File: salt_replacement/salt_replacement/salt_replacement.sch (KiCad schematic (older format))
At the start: 20 parts, among them J1 SALT chip package pins, Q1 MMBT9014C, U1 LM2596S-5, U2 MAX3232, U3 LM393

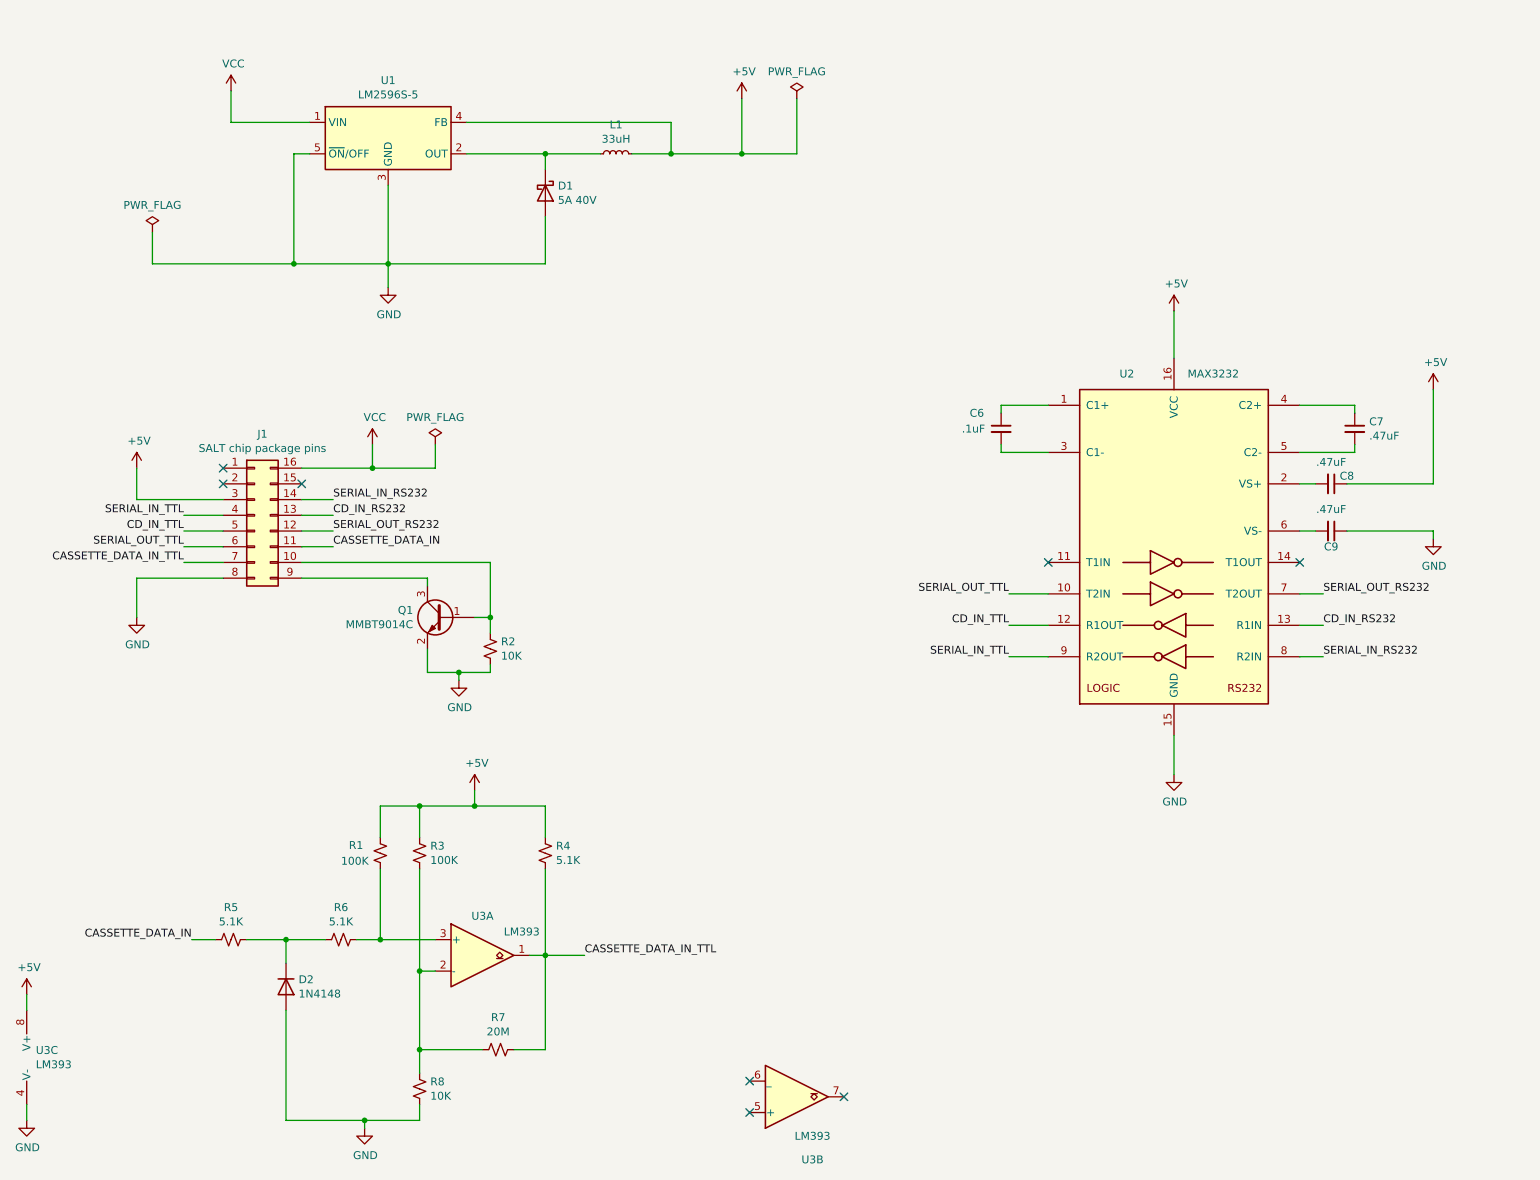
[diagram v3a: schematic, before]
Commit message: cleaned up schematic, added comments and added a PDF version of the schematic
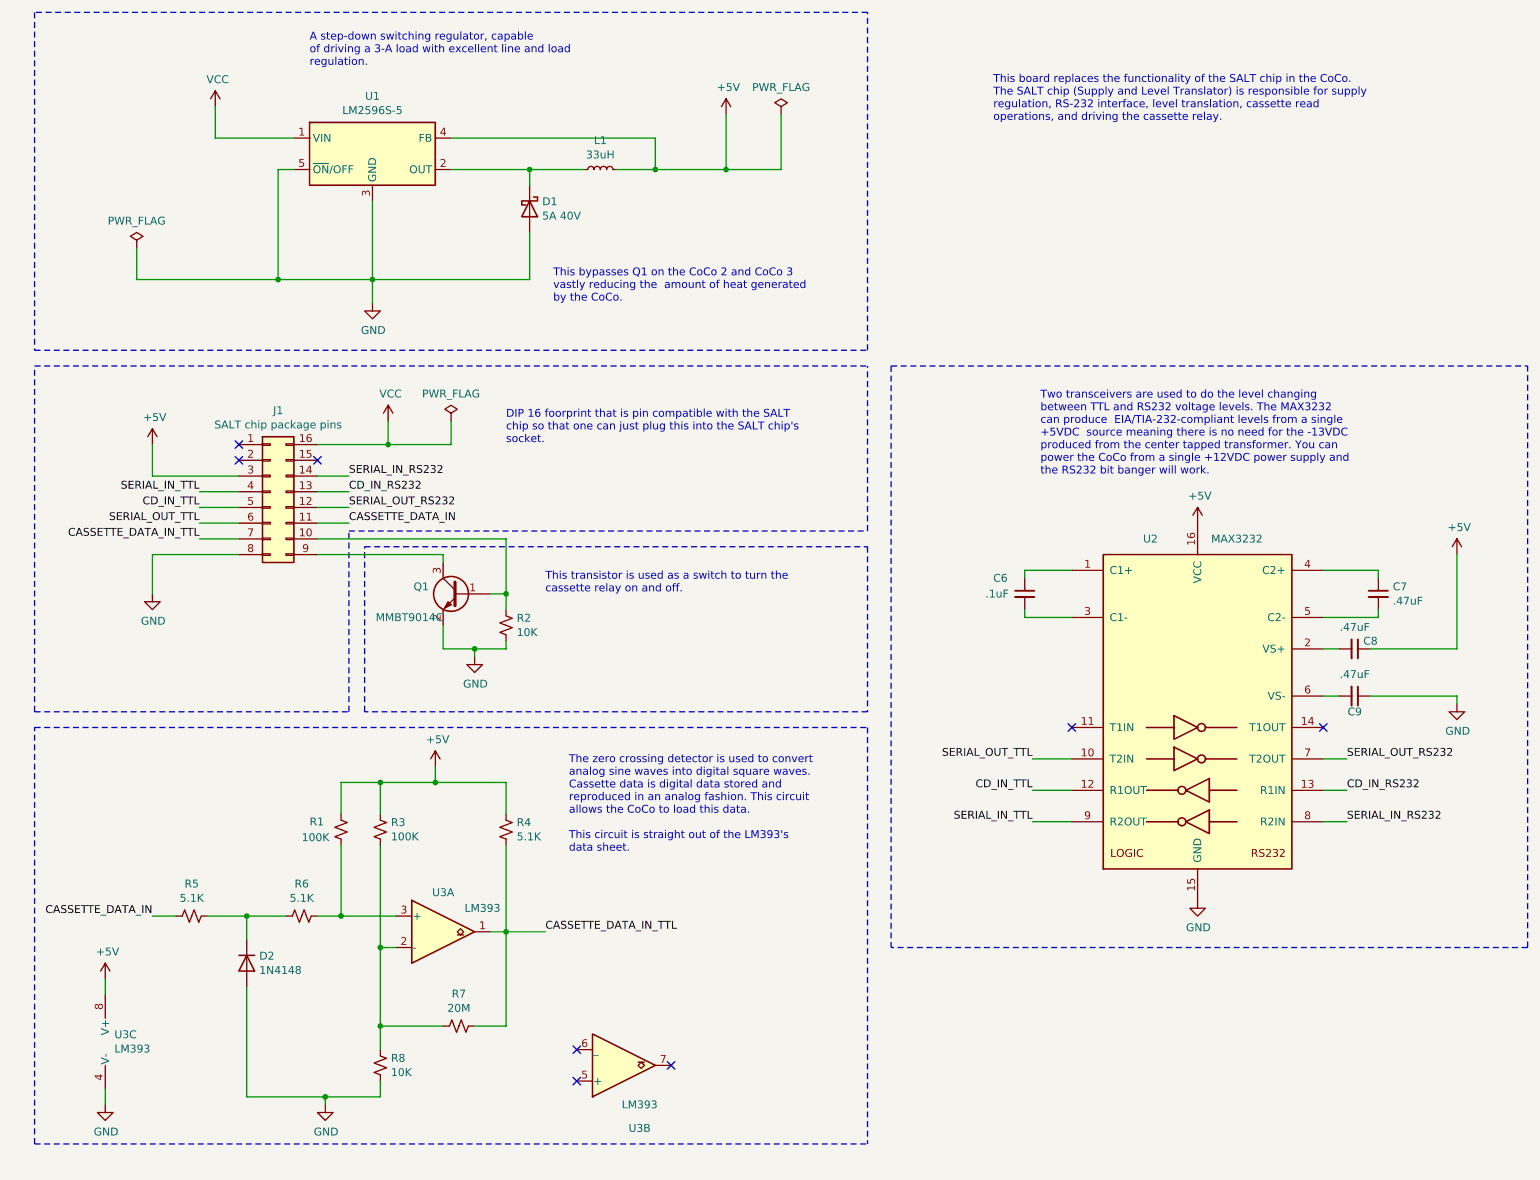
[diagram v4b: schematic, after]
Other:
- note added: "A step-down switching regulator, capable\nof driving a 3-A load with excellent line and load\nregulation."
- note added: "DIP 16 foorprint that is pin compatible with the SALT\nchip so that one can just plug this into the SALT chip's\nsocket."
- note added: "The zero crossing detector is used to convert\nanalog sine waves into digital square waves.\nCassette data is digital data stored and \nreproduced in an analog fashion. This circuit\nallows the CoCo to load this data.\n\nThis circuit is straight out of the LM393's\ndata sheet."
- note added: "This board replaces the functionality of the SALT chip in the CoCo. \nThe SALT chip (Supply and Level Translator) is responsible for supply\nregulation, RS-232 interface, level translation, cassette read\noperations, and driving the cassette relay."
- note added: "This bypasses Q1 on the CoCo 2 and CoCo 3\nvastly reducing the amount of heat generated\nby the CoCo."
- note added: "This transistor is used as a switch to turn the\ncassette relay on and off."
- note added: "Two transceivers are used to do the level changing\nbetween TTL and RS232 voltage levels. The MAX3232\ncan produce EIA/TIA-232-compliant levels from a single \n+5VDC source meaning there is no need for the -13VDC\nproduced from the center tapped transformer. You can\npower the CoCo from a single +12VDC power supply and\nthe RS232 bit banger will work."
- moved on the sheet: C6, C7, C8, C9, D1, D2, J1, L1, Q1, R1, R2, R3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
